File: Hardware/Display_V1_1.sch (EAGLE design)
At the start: 91 parts, among them IC1 STM32F030C6T, IC2 LM2623, IC3 MCP73831, IC4 LP2985M5, M1 WIRELESS-NRF24L01, Q1 BSS138, Q10 BSS138, Q11 IRLML5203, Q12 BSS138, Q13 IRLML5203, Q14 BSS138, Q15 IRLML5203, Q16 BSS138, Q17 IRLML5203, Q18 BC817-16LT1SMD, Q19 BC817-16LT1SMD, Q2 BSS138, Q3 BSS138, Q4 BSS138, Q5 BSS138, Q6 BSS138, Q7 BSS138, Q8 BSS138, Q9 IRLML5203, X1 MINI-USB-UX60-MB-5ST, Y1 8MHz

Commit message: last(?) changes
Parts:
- D2: device diode:DIODE-SOD323-W -> diode:DIODE-MINIMELF
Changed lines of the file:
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@@
 <grid distance="0.1" unitdist="inch" unit="inch" style="lines" multiple="1" display="no" altdistance="0.01" altunitdist="inch" altunit="inch"/>
 <layers>
-<layer number="1" name="Top" color="4" fill="1" visible="no" active="no"/>
-<layer number="2" name="Route2" color="1" fill="3" visible="no" active="no"/>
-<layer number="3" name="Route3" color="4" fill="3" visible="no" active="no"/>
-<layer number="14" name="Route14" color="1" fill="6" visible="no" active="no"/>
-<layer number="15" name="Route15" color="4" fill="6" visible="no" active="no"/>
-<layer number="16" name="Bottom" color="1" fill="1" visible="no" active="no"/>
-<layer number="17" name="Pads" color="2" fill="1" visible="no" active="no"/>
-<layer number="18" name="Vias" color="2" fill="1" visible="no" active="no"/>
-<layer number="19" name="Unrouted" color="6" fill="1" visible="no" active="no"/>
-<layer number="20" name="Dimension" color="15" fill="1" visible="no" active="no"/>
-<layer number="21" name="tPlace" color="7" fill="1" visible="no" active="no"/>
-<layer number="22" name="bPlace" color="7" fill="1" visible="no" active="no"/>
-<layer number="23" name="tOrigins" color="15" fill="1" visible="no" active="no"/>
-<layer number="24" name="bOrigins" color="15" fill="1" visible="no" active="no"/>
-<layer number="25" name="tNames" color="7" fill="1" visible="no" active="no"/>
-<layer number="26" name="bNames" color="7" fill="1" visible="no" active="no"/>
-<layer number="27" name="tValues" color="7" fill="1" visible="no" active="no"/>
-<layer number="28" name="bValues" color="7" fill="1" visible="no" active="no"/>
+<layer number="1" name="Top" color="4" fill="1" visible="yes" active="no"/>
+<layer number="2" name="Route2" color="1" fill="3" visible="yes" active="no"/>
+<layer number="3" name="Route3" color="4" fill="3" visible="yes" active="no"/>
+<layer number="14" name="Route14" color="1" fill="6" visible="yes" active="no"/>
+<layer number="15" name="Route15" color="4" fill="6" visible="yes" active="no"/>
+<layer number="16" name="Bottom" color="1" fill="1" visible="yes" active="no"/>
+<layer number="17" name="Pads" color="2" fill="1" visible="yes" active="no"/>
+<layer number="18" name="Vias" color="2" fill="1" visible="yes" active="no"/>
+<layer number="19" name="Unrouted" color="6" fill="1" visible="yes" active="no"/>
+<layer number="20" name="Dimension" color="15" fill="1" visible="yes" active="no"/>
+<layer number="21" name="tPlace" color="7" fill="1" visible="yes" active="no"/>
+<layer number="22" name="bPlace" color="7" fill="1" visible="yes" active="no"/>
+<layer number="23" name="tOrigins" color="15" fill="1" visible="yes" active="no"/>
+<layer number="24" name="bOrigins" color="15" fill="1" visible="yes" active="no"/>
+<layer number="25" name="tNames" color="7" fill="1" visible="yes" active="no"/>
+<layer number="26" name="bNames" color="7" fill="1" visible="yes" active="no"/>
+<layer number="27" name="tValues" color="7" fill="1" visible="yes" active="no"/>
+<layer number="28" name="bValues" color="7" fill="1" visible="yes" active="no"/>
 <layer number="29" name="tStop" color="7" fill="3" visible="no" active="no"/>
 <layer number="30" name="bStop" color="7" fill="6" visible="no" active="no"/>
@@
 <layer number="35" name="tGlue" color="7" fill="4" visible="no" active="no"/>
 <layer number="36" name="bGlue" color="7" fill="5" visible="no" active="no"/>
-<layer number="37" name="tTest" color="7" fill="1" visible="no" active="no"/>
-<layer number="38" name="bTest" color="7" fill="1" visible="no" active="no"/>
+<layer number="37" name="tTest" color="7" fill="1" visible="yes" active="no"/>
+<layer number="38" name="bTest" color="7" fill="1" visible="yes" active="no"/>
 <layer number="39" name="tKeepout" color="4" fill="11" visible="no" active="no"/>
 <layer number="40" name="bKeepout" color="1" fill="11" visible="no" active="no"/>
@@
 <layer number="44" name="Drills" color="7" fill="1" visible="no" active="no"/>
 <layer number="45" name="Holes" color="7" fill="1" visible="no" active="no"/>
-<layer number="46" name="Milling" color="3" fill="1" visible="no" active="no"/>
-<layer number="47" name="Measures" color="7" fill="1" visible="no" active="no"/>
-<layer number="48" name="Document" color="7" fill="1" visible="no" active="no"/>
-<layer number="49" name="Reference" color="7" fill="1" visible="no" active="no"/>
-<layer number="50" name="dxf" color="7" fill="1" visible="no" active="no"/>
-<layer number="51" name="tDocu" color="7" fill="1" visible="no" active="no"/>
-<layer number="52" name="bDocu" color="7" fill="1" visible="no" active="no"/>
-<layer number="53" name="tGND_GNDA" color="7" fill="1" visible="no" active="no"/>
-<layer number="54" name="bGND_GNDA" color="7" fill="1" visible="no" active="no"/>
-<layer number="56" name="wert" color="7" fill="1" visible="no" active="no"/>
+<layer number="46" name="Milling" color="3" fill="1" visible="yes" active="no"/>
+<layer number="47" name="Measures" color="7" fill="1" visible="yes" active="no"/>
+<layer number="48" name="Document" color="7" fill="1" visible="yes" active="no"/>
+<layer number="49" name="Reference" color="7" fill="1" visible="yes" active="no"/>
+<layer number="50" name="dxf" color="7" fill="1" visible="yes" active="no"/>
+<layer number="51" name="tDocu" color="7" fill="1" visible="yes" active="no"/>
+<layer number="52" name="bDocu" color="7" fill="1" visible="yes" active="no"/>
+<layer number="53" name="tGND_GNDA" color="7" fill="1" visible="yes" active="no"/>
+<layer number="54" name="bGND_GNDA" color="7" fill="1" visible="yes" active="no"/>
+<layer number="56" name="wert" color="7" fill="1" visible="yes" active="no"/>
 <layer number="90" name="Modules" color="5" fill="1" visible="yes" active="yes"/>
 <layer number="91" name="Nets" color="2" fill="1" visible="yes" active="yes"/>
@@
 <part name="R18" library="rcl" deviceset="R-EU_" device="R0603" value="4k7"/>
 <part name="R19" library="rcl" deviceset="R-EU_" device="R0603" value="100k"/>
-<part name="D2" library="diode" deviceset="DIODE-" device="SOD323-W" value="1N4148"/>
+<part name="D2" library="diode" deviceset="DIODE-" device="MINIMELF" value="1N4148"/>
 <part name="GND30" library="supply1" deviceset="GND" device=""/>
 <part name="Q19" library="transistor-npn" deviceset="BC817*" device="SMD" technology="-16LT1"/>

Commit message: Final PCB changes
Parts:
- IC2: value LM2623 -> LM2623MM; device v-reg-3:LM2623 -> v-reg-3:LM2623MM
- R1: value 150 -> 120
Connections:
- net N$16 renamed V+
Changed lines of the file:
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@@
 <grid distance="0.1" unitdist="inch" unit="inch" style="lines" multiple="1" display="no" altdistance="0.01" altunitdist="inch" altunit="inch"/>
 <layers>
-<layer number="1" name="Top" color="4" fill="1" visible="yes" active="no"/>
-<layer number="2" name="Route2" color="1" fill="3" visible="yes" active="no"/>
-<layer number="3" name="Route3" color="4" fill="3" visible="yes" active="no"/>
-<layer number="14" name="Route14" color="1" fill="6" visible="yes" active="no"/>
-<layer number="15" name="Route15" color="4" fill="6" visible="yes" active="no"/>
-<layer number="16" name="Bottom" color="1" fill="1" visible="yes" active="no"/>
-<layer number="17" name="Pads" color="2" fill="1" visible="yes" active="no"/>
-<layer number="18" name="Vias" color="2" fill="1" visible="yes" active="no"/>
-<layer number="19" name="Unrouted" color="6" fill="1" visible="yes" active="no"/>
-<layer number="20" name="Dimension" color="15" fill="1" visible="yes" active="no"/>
-<layer number="21" name="tPlace" color="7" fill="1" visible="yes" active="no"/>
-<layer number="22" name="bPlace" color="7" fill="1" visible="yes" active="no"/>
-<layer number="23" name="tOrigins" color="15" fill="1" visible="yes" active="no"/>
-<layer number="24" name="bOrigins" color="15" fill="1" visible="yes" active="no"/>
-<layer number="25" name="tNames" color="7" fill="1" visible="yes" active="no"/>
-<layer number="26" name="bNames" color="7" fill="1" visible="yes" active="no"/>
-<layer number="27" name="tValues" color="7" fill="1" visible="yes" active="no"/>
-<layer number="28" name="bValues" color="7" fill="1" visible="yes" active="no"/>
+<layer number="1" name="Top" color="4" fill="1" visible="no" active="no"/>
+<layer number="2" name="Route2" color="1" fill="3" visible="no" active="no"/>
+<layer number="3" name="Route3" color="4" fill="3" visible="no" active="no"/>
+<layer number="14" name="Route14" color="1" fill="6" visible="no" active="no"/>
+<layer number="15" name="Route15" color="4" fill="6" visible="no" active="no"/>
+<layer number="16" name="Bottom" color="1" fill="1" visible="no" active="no"/>
+<layer number="17" name="Pads" color="2" fill="1" visible="no" active="no"/>
+<layer number="18" name="Vias" color="2" fill="1" visible="no" active="no"/>
+<layer number="19" name="Unrouted" color="6" fill="1" visible="no" active="no"/>
+<layer number="20" name="Dimension" color="15" fill="1" visible="no" active="no"/>
+<layer number="21" name="tPlace" color="7" fill="1" visible="no" active="no"/>
+<layer number="22" name="bPlace" color="7" fill="1" visible="no" active="no"/>
+<layer number="23" name="tOrigins" color="15" fill="1" visible="no" active="no"/>
+<layer number="24" name="bOrigins" color="15" fill="1" visible="no" active="no"/>
+<layer number="25" name="tNames" color="7" fill="1" visible="no" active="no"/>
+<layer number="26" name="bNames" color="7" fill="1" visible="no" active="no"/>
+<layer number="27" name="tValues" color="7" fill="1" visible="no" active="no"/>
+<layer number="28" name="bValues" color="7" fill="1" visible="no" active="no"/>
 <layer number="29" name="tStop" color="7" fill="3" visible="no" active="no"/>
 <layer number="30" name="bStop" color="7" fill="6" visible="no" active="no"/>
@@
 <layer number="35" name="tGlue" color="7" fill="4" visible="no" active="no"/>
 <layer number="36" name="bGlue" color="7" fill="5" visible="no" active="no"/>
-<layer number="37" name="tTest" color="7" fill="1" visible="yes" active="no"/>
-<layer number="38" name="bTest" color="7" fill="1" visible="yes" active="no"/>
+<layer number="37" name="tTest" color="7" fill="1" visible="no" active="no"/>
+<layer number="38" name="bTest" color="7" fill="1" visible="no" active="no"/>
 <layer number="39" name="tKeepout" color="4" fill="11" visible="no" active="no"/>
 <layer number="40" name="bKeepout" color="1" fill="11" visible="no" active="no"/>
@@
 <layer number="44" name="Drills" color="7" fill="1" visible="no" active="no"/>
 <layer number="45" name="Holes" color="7" fill="1" visible="no" active="no"/>
-<layer number="46" name="Milling" color="3" fill="1" visible="yes" active="no"/>
-<layer number="47" name="Measures" color="7" fill="1" visible="yes" active="no"/>
-<layer number="48" name="Document" color="7" fill="1" visible="yes" active="no"/>
-<layer number="49" name="Reference" color="7" fill="1" visible="yes" active="no"/>
-<layer number="50" name="dxf" color="7" fill="1" visible="yes" active="no"/>
-<layer number="51" name="tDocu" color="7" fill="1" visible="yes" active="no"/>
-<layer number="52" name="bDocu" color="7" fill="1" visible="yes" active="no"/>
-<layer number="53" name="tGND_GNDA" color="7" fill="1" visible="yes" active="no"/>
-<layer number="54" name="bGND_GNDA" color="7" fill="1" visible="yes" active="no"/>
-<layer number="56" name="wert" color="7" fill="1" visible="yes" active="no"/>
+<layer number="46" name="Milling" color="3" fill="1" visible="no" active="no"/>
+<layer number="47" name="Measures" color="7" fill="1" visible="no" active="no"/>
+<layer number="48" name="Document" color="7" fill="1" visible="no" active="no"/>
+<layer number="49" name="Reference" color="7" fill="1" visible="no" active="no"/>
+<layer number="50" name="dxf" color="7" fill="1" visible="no" active="no"/>
+<layer number="51" name="tDocu" color="7" fill="1" visible="no" active="no"/>
+<layer number="52" name="bDocu" color="7" fill="1" visible="no" active="no"/>
+<layer number="53" name="tGND_GNDA" color="7" fill="1" visible="no" active="no"/>
+<layer number="54" name="bGND_GNDA" color="7" fill="1" visible="no" active="no"/>
+<layer number="56" name="wert" color="7" fill="1" visible="no" active="no"/>
 <layer number="90" name="Modules" color="5" fill="1" visible="yes" active="yes"/>
 <layer number="91" name="Nets" color="2" fill="1" visible="yes" active="yes"/>
@@
 <part name="C6" library="rcl" deviceset="C-EU" device="C0603" value="100n"/>
 <part name="C12" library="rcl" deviceset="C-EU" device="C0603" value="1u"/>
-<part name="R1" library="rcl" deviceset="R-EU_" device="R1206" value="150"/>
+<part name="R1" library="rcl" deviceset="R-EU_" device="R1206" value="120"/>
 <part name="Q1" library="transistor-small-signal" deviceset="BSS123" device="" value="BSS138"/>
 <part name="GND7" library="supply1" deviceset="GND" device=""/>
@@
 <part name="P+12" library="supply1" deviceset="+12V" device=""/>
 <part name="GND1" library="supply1" deviceset="GND" device=""/>
-<part name="IC2" library="v-reg-3" deviceset="LM2623" device=""/>
+<part name="IC2" library="v-reg-3" deviceset="LM2623" device="MM"/>
 <part name="GND6" library="supply1" deviceset="GND" device=""/>
 <part name="C3" library="rcl" deviceset="C-EU" device="C0603" value="4p7"/>
@@
 </segment>
 </net>
-<net name="N$16" class="0">
+<net name="V+" class="0">
 <segment>
 <pinref part="IC3" gate="G$1" pin="VBAT"/>

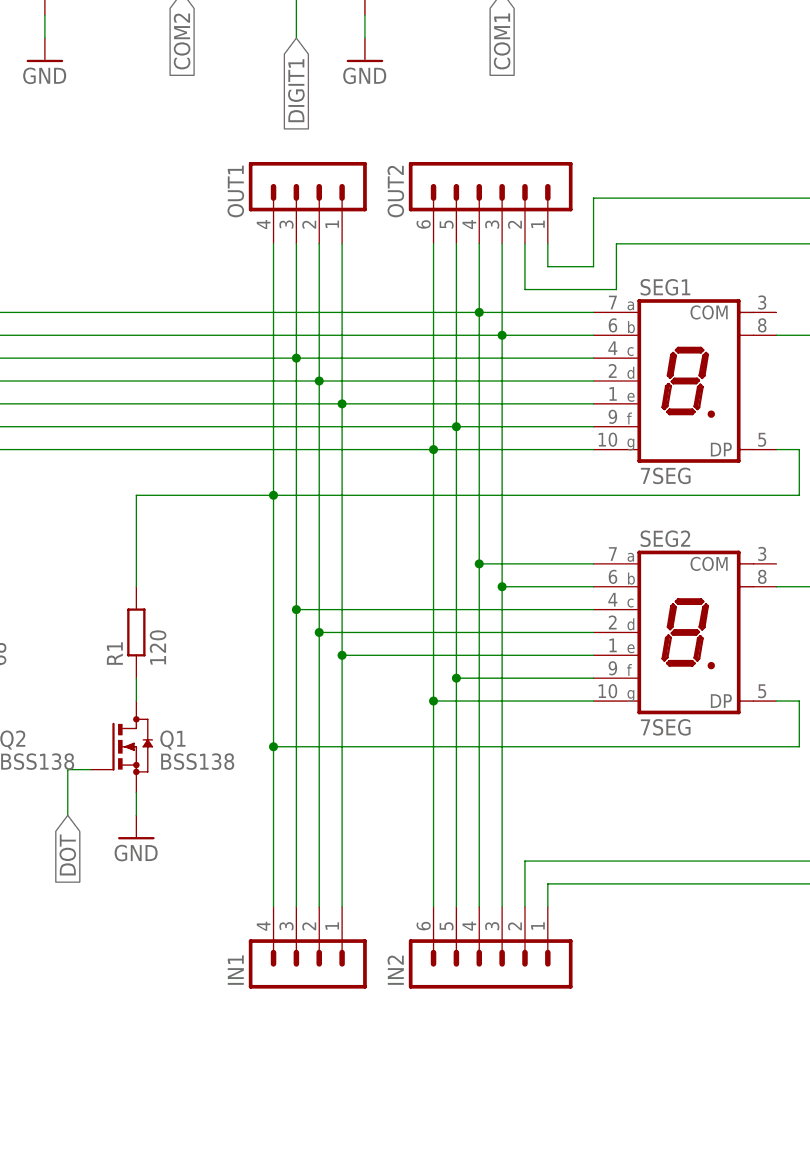
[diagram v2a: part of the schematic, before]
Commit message: Slight changes for easier fabrication
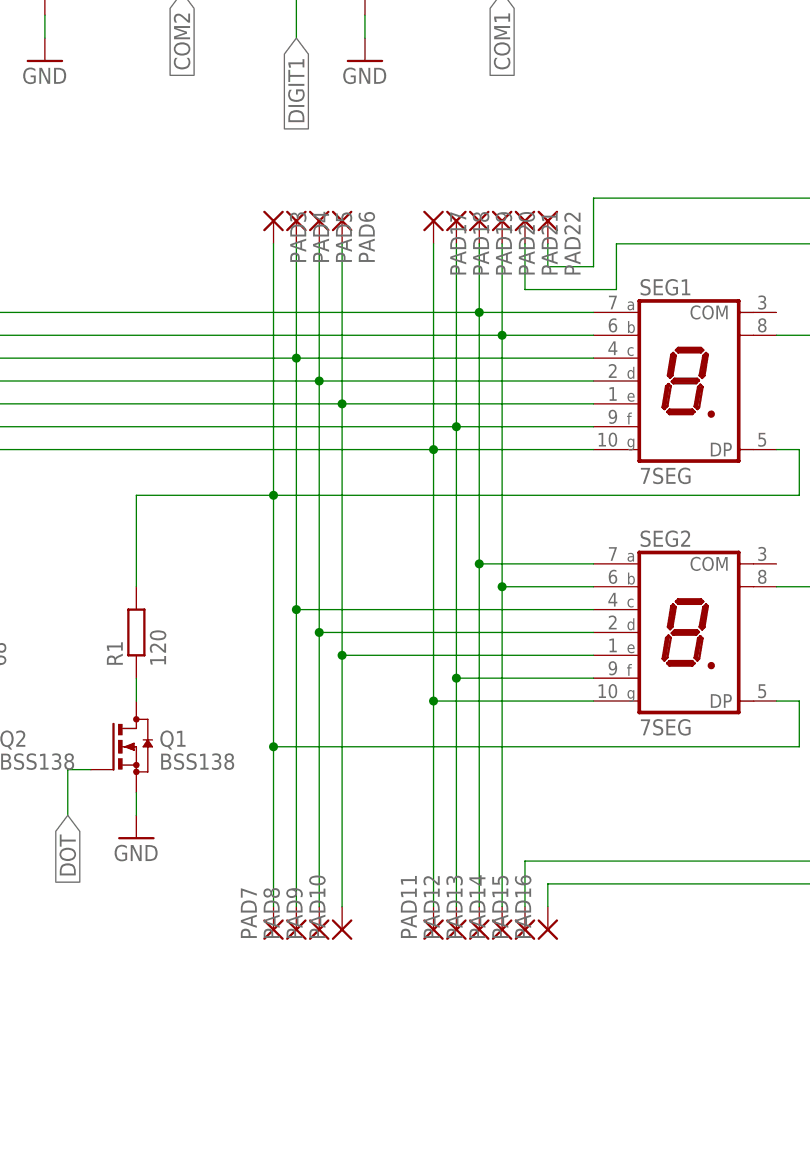
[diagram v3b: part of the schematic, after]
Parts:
- removed IN1, OUT1: (no value), con-lstb:MA04-1
- removed IN2, OUT2: (no value), con-lstb:MA06-1
- added PAD10, PAD11, PAD12, PAD13, PAD14, PAD15, PAD16, PAD17, PAD18, PAD19, PAD20, PAD21, PAD22, PAD3, PAD4, PAD5, PAD6, PAD7, PAD8, PAD9: (no value), wirepad:SMD2
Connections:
- net COM1: now also PAD15.P; no longer IN2.2
- net COM2: now also PAD16.P; no longer IN2.1
- net COM3: now also PAD21.P; no longer OUT2.2
- net COM4: now also PAD22.P; no longer OUT2.1
- net DP: now also PAD3.P, PAD7.P; no longer IN1.4, OUT1.4
- net SEG_A: now also PAD13.P, PAD19.P; no longer IN2.4, OUT2.4
- net SEG_B: now also PAD14.P, PAD20.P; no longer IN2.3, OUT2.3
- net SEG_C: now also PAD4.P, PAD8.P; no longer IN1.3, OUT1.3
- net SEG_D: now also PAD5.P, PAD9.P; no longer IN1.2, OUT1.2
- net SEG_E: now also PAD10.P, PAD6.P; no longer IN1.1, OUT1.1
- net SEG_F: now also PAD12.P, PAD18.P; no longer IN2.5, OUT2.5
- net SEG_G: now also PAD11.P, PAD17.P; no longer IN2.6, OUT2.6

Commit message: Bugfixes and improvements, basic system working
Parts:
- R10, R11, R12, R9: value 100k -> 3k3
- R4: value 68 -> 120
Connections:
- removed net DOT: IC1MCU.PB9, Q1.G
- new net S_DOT: IC1MCU.PA15, Q4.G
- net DP: now also PAD10.P, PAD6.P, R4.2, SEG1.E, SEG2.E; no longer PAD3.P, PAD7.P, R1.2, SEG1.DP, SEG2.DP
- net SEG_C: now also PAD5.P, PAD9.P, R5.2, SEG1.D, SEG2.D; no longer PAD4.P, PAD8.P, R6.2, SEG1.C, SEG2.C
- net SEG_D: now also PAD4.P, PAD8.P, R6.2, SEG1.C, SEG2.C; no longer PAD5.P, PAD9.P, R5.2, SEG1.D, SEG2.D
- net SEG_E: now also PAD3.P, PAD7.P, R1.2, SEG1.DP, SEG2.DP; no longer PAD10.P, PAD6.P, R4.2, SEG1.E, SEG2.E
- net S_C: now also IC1MCU.PF6, Q5.G; no longer IC1MCU.PB8, Q6.G
- net S_D: now also IC1MCU.PB8, Q6.G; no longer IC1MCU.PF6, Q5.G
- net S_E: now also IC1MCU.PB9, Q1.G; no longer IC1MCU.PA15, Q4.G
